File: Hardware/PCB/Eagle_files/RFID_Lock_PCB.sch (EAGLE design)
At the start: 37 parts, among them IC1 74AHCT125, J3 Servo, K1 351, T2 2N2222

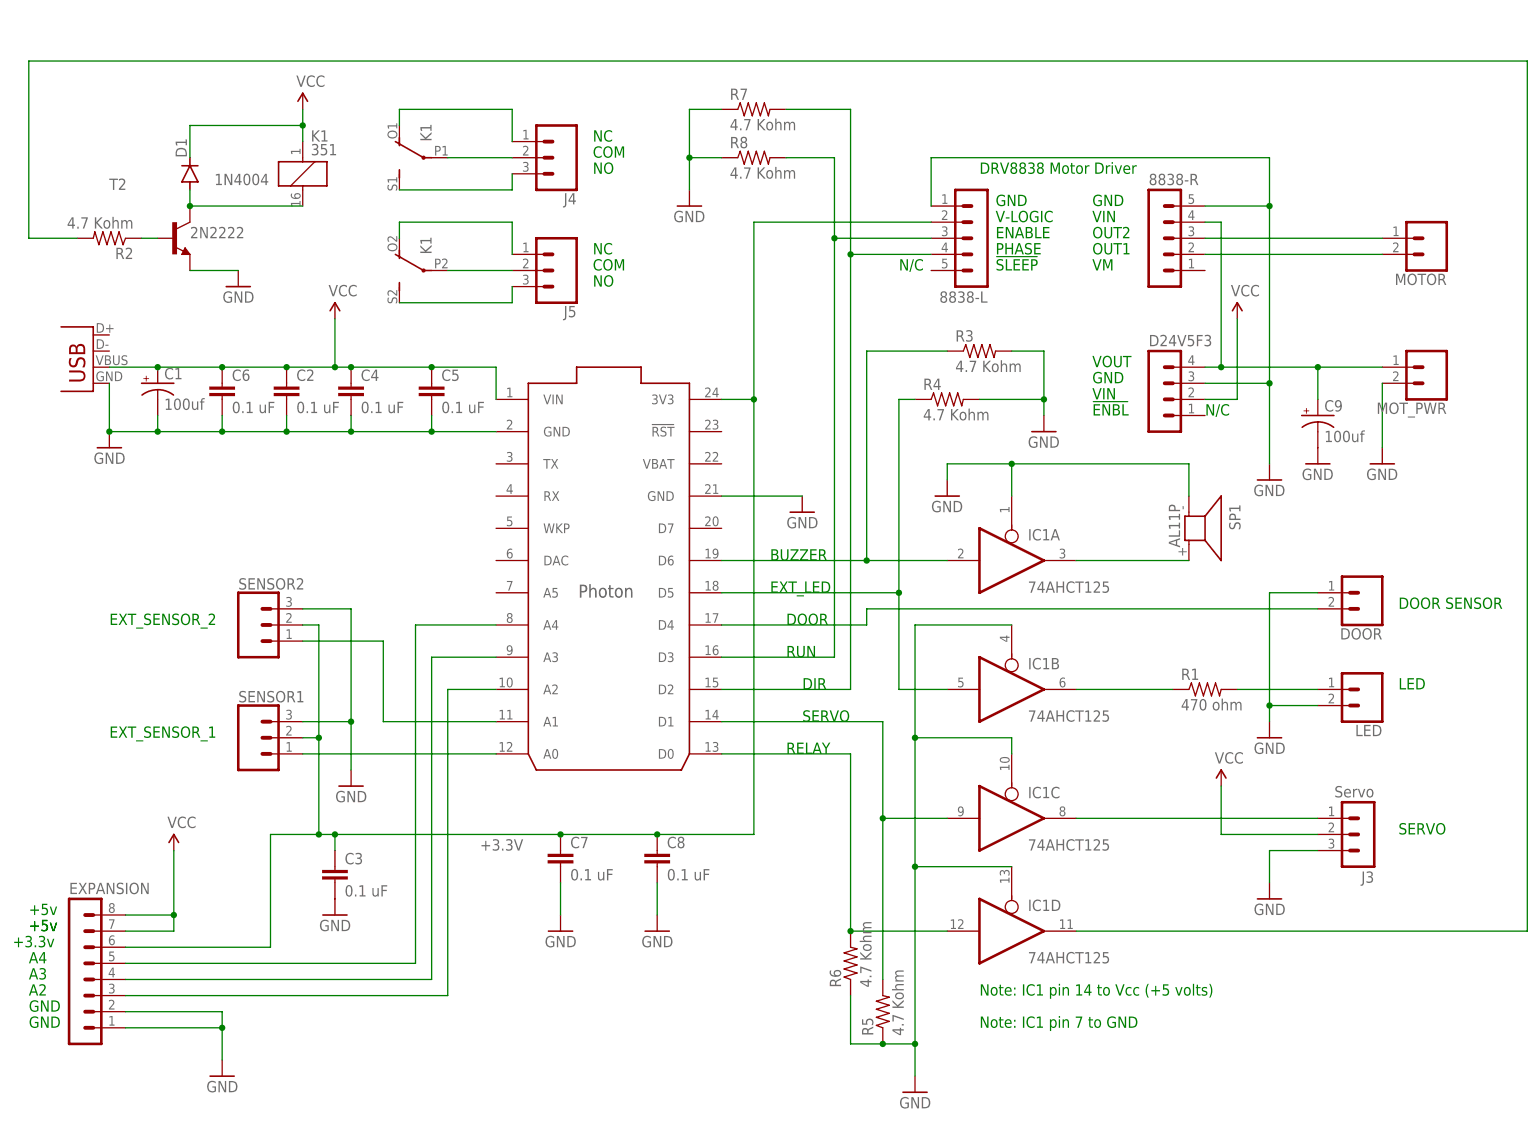
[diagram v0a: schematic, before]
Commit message: Updated schematic
Updated board schematic to wire one relay pole to support a solenoid.  The second relay pole is left for general purpose use.
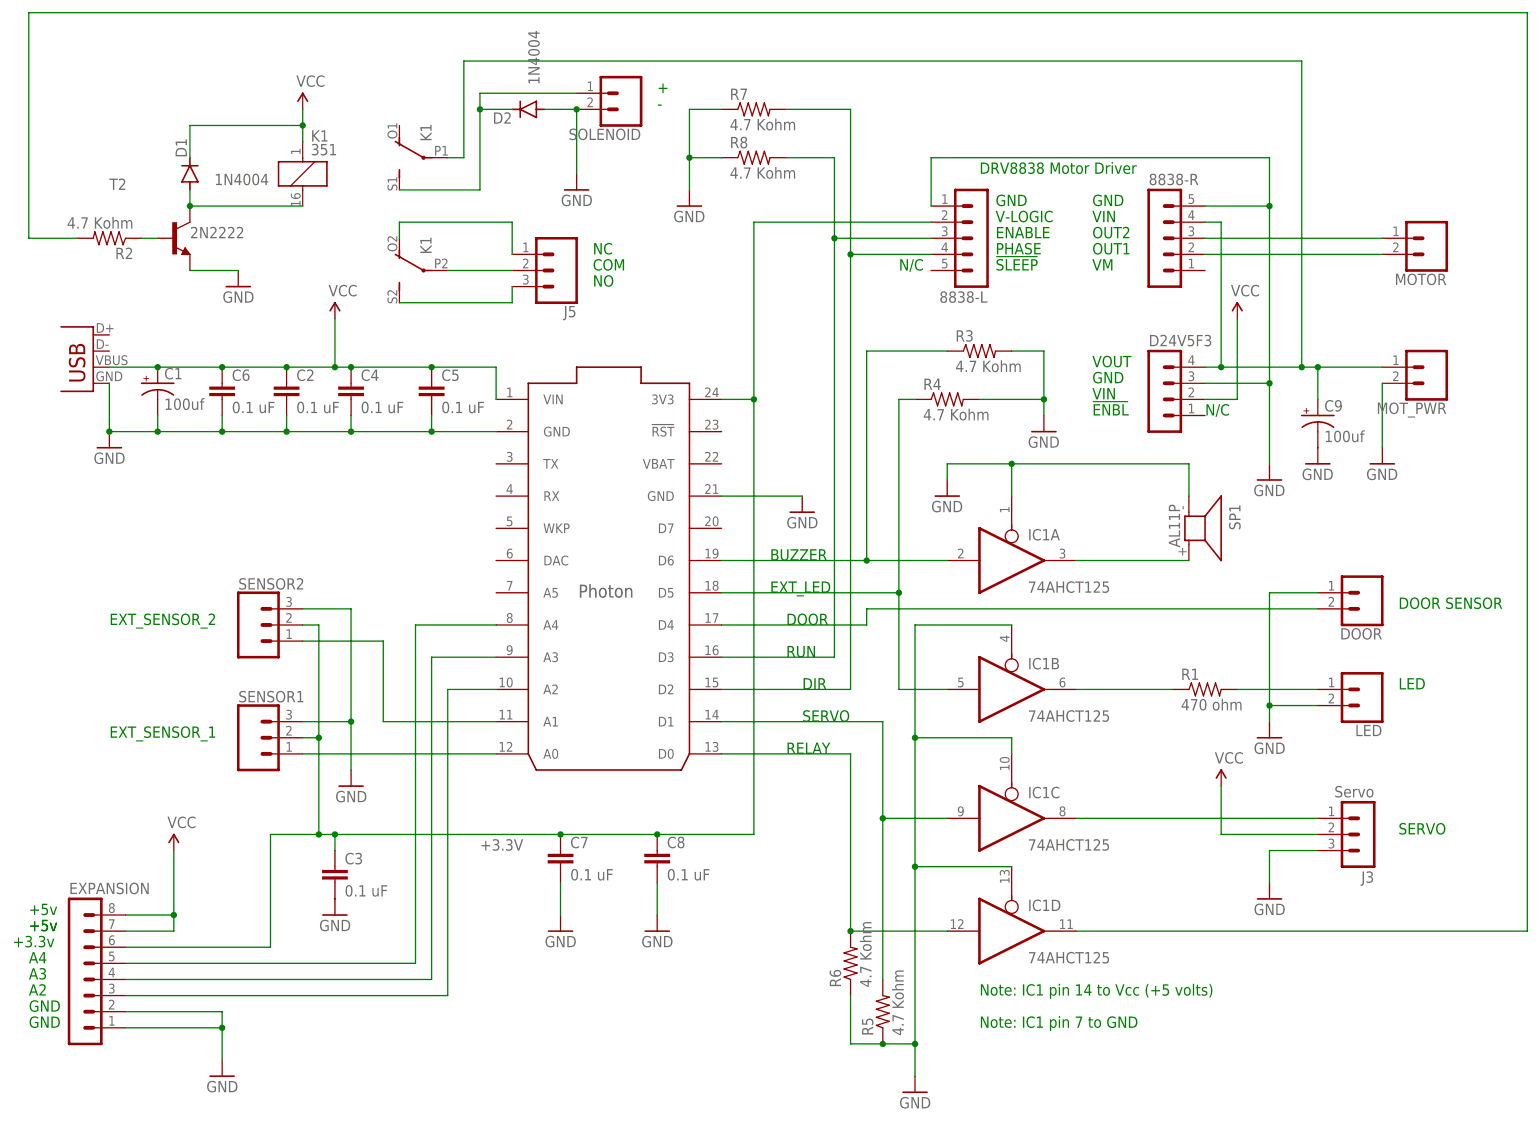
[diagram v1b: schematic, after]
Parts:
- removed J4: (no value), SparkFun-Connectors:CONN_03SCREW
- added D2: 1N4004, diode:1N4004
- added SOLENOID: (no value), SparkFun-Connectors:CONN_023.5MM
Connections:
- removed net N$24: J4.1, K12.O
- removed net N$25: J4.3, K12.S
- net GND: now also D2.A, SOLENOID.2
- net N$22: now also D2.C, K12.S, SOLENOID.1; no longer J4.2, K12.P
- net N$6: now also K12.P
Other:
- note added: "+"
- note added: "-"
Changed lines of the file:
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@@
 <part name="SUPPLY5" library="SparkFun-Aesthetics" deviceset="VCC" device=""/>
 <part name="D1" library="diode" library_urn="urn:adsk.eagle:library:210" deviceset="1N4004" device="" package3d_urn="urn:adsk.eagle:package:43336/1"/>
-<part name="J4" library="SparkFun-Connectors" library_urn="urn:adsk.eagle:library:513" deviceset="CONN_03" device="SCREW" package3d_urn="urn:adsk.eagle:package:38072/1"/>
 <part name="J5" library="SparkFun-Connectors" library_urn="urn:adsk.eagle:library:513" deviceset="CONN_03" device="SCREW" package3d_urn="urn:adsk.eagle:package:38072/1"/>
 <part name="C9" library="SparkFun-Capacitors" deviceset="CAP_POL" device="PTH1" value="100uf"/>
@@
 <part name="R8" library="rcl" deviceset="R-US_" device="0309/12" value="4.7 Kohm"/>
 <part name="GND17" library="SparkFun-Aesthetics" deviceset="GND" device=""/>
+<part name="SOLENOID" library="SparkFun-Connectors" library_urn="urn:adsk.eagle:library:513" deviceset="CONN_02" device="3.5MM" package3d_urn="urn:adsk.eagle:package:38050/1"/>
+<part name="GND18" library="SparkFun-Aesthetics" deviceset="GND" device=""/>
+<part name="D2" library="diode" library_urn="urn:adsk.eagle:library:210" deviceset="1N4004" device="" package3d_urn="urn:adsk.eagle:package:43336/1"/>
 </parts>
 <sheets>
@@
 <text x="-99.06" y="2.54" size="1.778" layer="91">A3</text>
 <text x="-99.06" y="5.08" size="1.778" layer="91">A4</text>
-<text x="-10.16" y="134.62" size="1.778" layer="91">NC</text>
-<text x="-10.16" y="132.08" size="1.778" layer="91">COM</text>
-<text x="-10.16" y="129.54" size="1.778" layer="91">NO</text>
 <text x="-10.16" y="116.84" size="1.778" layer="91">NC</text>
 <text x="-10.16" y="114.3" size="1.778" layer="91">COM</text>
 <text x="-10.16" y="111.76" size="1.778" layer="91">NO</text>
+<text x="0" y="142.24" size="1.778" layer="91">+</text>
+<text x="0" y="139.7" size="1.778" layer="91">-</text>
 </plain>
 <instances>
@@
 <attribute name="VALUE" x="-61.1886" y="129.54" size="1.778" layer="96" rot="R180"/>
 </instance>
-<instance part="J4" gate="J$1" x="-15.24" y="132.08" smashed="yes" rot="R180">
-<attribute name="VALUE" x="-12.7" y="139.446" size="1.778" layer="96" font="vector" rot="R180"/>
-<attribute name="NAME" x="-12.7" y="126.492" size="1.778" layer="95" font="vector" rot="R180"/>
-</instance>
 <instance part="J5" gate="J$1" x="-15.24" y="114.3" smashed="yes" rot="R180">
 <attribute name="VALUE" x="-12.7" y="121.666" size="1.778" layer="96" font="vector" rot="R180"/>
@@
 <instance part="GND17" gate="1" x="5.08" y="124.46" smashed="yes">
 <attribute name="VALUE" x="2.54" y="121.92" size="1.778" layer="96"/>
+</instance>
+<instance part="SOLENOID" gate="G$1" x="-5.08" y="142.24" smashed="yes" rot="R180">
+<attribute name="VALUE" x="-2.54" y="147.066" size="1.778" layer="96" font="vector" rot="R180"/>
+<attribute name="NAME" x="-2.54" y="136.652" size="1.778" layer="95" font="vector" rot="R180"/>
+</instance>
+<instance part="GND18" gate="1" x="-12.7" y="127" smashed="yes" rot="MR0">
+<attribute name="VALUE" x="-10.16" y="124.46" size="1.778" layer="96" rot="MR0"/>
+</instance>
+<instance part="D2" gate="1" x="-20.32" y="139.7" smashed="yes" rot="R180">
+<attribute name="NAME" x="-22.86" y="139.2174" size="1.778" layer="95" rot="R180"/>
+<attribute name="VALUE" x="-20.32" y="152.1714" size="1.778" layer="96" rot="R270"/>
 </instance>
 </instances>
@@
 <wire x1="10.16" y1="132.08" x2="5.08" y2="132.08" width="0.1524" layer="91"/>
 <junction x="5.08" y="132.08"/>
+</segment>
+<segment>
+<pinref part="SOLENOID" gate="G$1" pin="2"/>
+<pinref part="GND18" gate="1" pin="GND"/>
+<wire x1="-12.7" y1="139.7" x2="-12.7" y2="129.54" width="0.1524" layer="91"/>
+<pinref part="D2" gate="1" pin="A"/>
+<wire x1="-12.7" y1="139.7" x2="-17.78" y2="139.7" width="0.1524" layer="91"/>
+<junction x="-12.7" y="139.7"/>
 </segment>
 </net>
@@
 <wire x1="88.9" y1="121.92" x2="86.36" y2="121.92" width="0.1524" layer="91"/>
 <pinref part="MOT_PWR" gate="G$1" pin="1"/>
-<wire x1="88.9" y1="99.06" x2="104.14" y2="99.06" width="0.1524" layer="91"/>
+<wire x1="88.9" y1="99.06" x2="101.6" y2="99.06" width="0.1524" layer="91"/>
 <junction x="88.9" y="99.06"/>
 <pinref part="C9" gate="G$1" pin="+"/>
+<wire x1="101.6" y1="99.06" x2="104.14" y2="99.06" width="0.1524" layer="91"/>
 <wire x1="104.14" y1="99.06" x2="114.3" y2="99.06" width="0.1524" layer="91"/>
 <wire x1="104.14" y1="93.98" x2="104.14" y2="99.06" width="0.1524" layer="91"/>
 <junction x="104.14" y="99.06"/>
+<wire x1="101.6" y1="99.06" x2="101.6" y2="147.32" width="0.1524" layer="91"/>
+<wire x1="101.6" y1="147.32" x2="-30.48" y2="147.32" width="0.1524" layer="91"/>
+<junction x="101.6" y="99.06"/>
+<wire x1="-30.48" y1="147.32" x2="-30.48" y2="132.08" width="0.1524" layer="91"/>
+<pinref part="K1" gate="2" pin="P"/>
+<wire x1="-30.48" y1="132.08" x2="-33.02" y2="132.08" width="0.1524" layer="91"/>
 </segment>
 </net>
@@
 <pinref part="IC1" gate="D" pin="O"/>
 <wire x1="66.04" y1="10.16" x2="137.16" y2="10.16" width="0.1524" layer="91"/>
-<wire x1="137.16" y1="10.16" x2="137.16" y2="147.32" width="0.1524" layer="91"/>
-<wire x1="137.16" y1="147.32" x2="-99.06" y2="147.32" width="0.1524" layer="91"/>
-<wire x1="-99.06" y1="147.32" x2="-99.06" y2="119.38" width="0.1524" layer="91"/>
+<wire x1="137.16" y1="10.16" x2="137.16" y2="154.94" width="0.1524" layer="91"/>
+<wire x1="137.16" y1="154.94" x2="-99.06" y2="154.94" width="0.1524" layer="91"/>
+<wire x1="-99.06" y1="154.94" x2="-99.06" y2="119.38" width="0.1524" layer="91"/>
 <pinref part="R2" gate="G$1" pin="2"/>
 <wire x1="-99.06" y1="119.38" x2="-91.44" y2="119.38" width="0.1524" layer="91"/>
@@
 </segment>
 </net>
-<net name="N$22" class="0">
-<segment>
-<pinref part="K1" gate="2" pin="P"/>
-<pinref part="J4" gate="J$1" pin="2"/>
-<wire x1="-33.02" y1="132.08" x2="-22.86" y2="132.08" width="0.1524" layer="91"/>
-</segment>
-</net>
-<net name="N$24" class="0">
-<segment>
-<pinref part="K1" gate="2" pin="O"/>
-<wire x1="-40.64" y1="137.16" x2="-40.64" y2="139.7" width="0.1524" layer="91"/>
-<wire x1="-40.64" y1="139.7" x2="-22.86" y2="139.7" width="0.1524" layer="91"/>
-<pinref part="J4" gate="J$1" pin="1"/>
-<wire x1="-22.86" y1="139.7" x2="-22.86" y2="134.62" width="0.1524" layer="91"/>
-</segment>
-</net>
-<net name="N$25" class="0">
-<segment>
-<pinref part="K1" gate="2" pin="S"/>
-<pinref part="J4" gate="J$1" pin="3"/>
-<wire x1="-40.64" y1="127" x2="-22.86" y2="127" width="0.1524" layer="91"/>
-<wire x1="-22.86" y1="127" x2="-22.86" y2="129.54" width="0.1524" layer="91"/>
-</segment>
-</net>
 <net name="N$26" class="0">
 <segment>
@@
 </segment>
 </net>
+<net name="N$22" class="0">
+<segment>
+<pinref part="SOLENOID" gate="G$1" pin="1"/>
+<wire x1="-12.7" y1="142.24" x2="-27.94" y2="142.24" width="0.1524" layer="91"/>
+<pinref part="K1" gate="2" pin="S"/>
+<wire x1="-40.64" y1="127" x2="-27.94" y2="127" width="0.1524" layer="91"/>
+<wire x1="-27.94" y1="127" x2="-27.94" y2="139.7" width="0.1524" layer="91"/>
+<pinref part="D2" gate="1" pin="C"/>
+<wire x1="-27.94" y1="139.7" x2="-27.94" y2="142.24" width="0.1524" layer="91"/>
+<wire x1="-22.86" y1="139.7" x2="-27.94" y2="139.7" width="0.1524" layer="91"/>
+<junction x="-27.94" y="139.7"/>
+</segment>
+</net>
